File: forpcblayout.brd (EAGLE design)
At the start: 100 x 80 mm, 51 parts, among them J1 3x2 M, J2 S2B-PH-SM4-TB(LF)(SN), J3 629105136821, SW1 AYZ0202AGRLC, SW2 !RESET, U1 MCP73831, U2 MIC5219, U3 ATMEGA32U4-AUR, X2 16 MHz

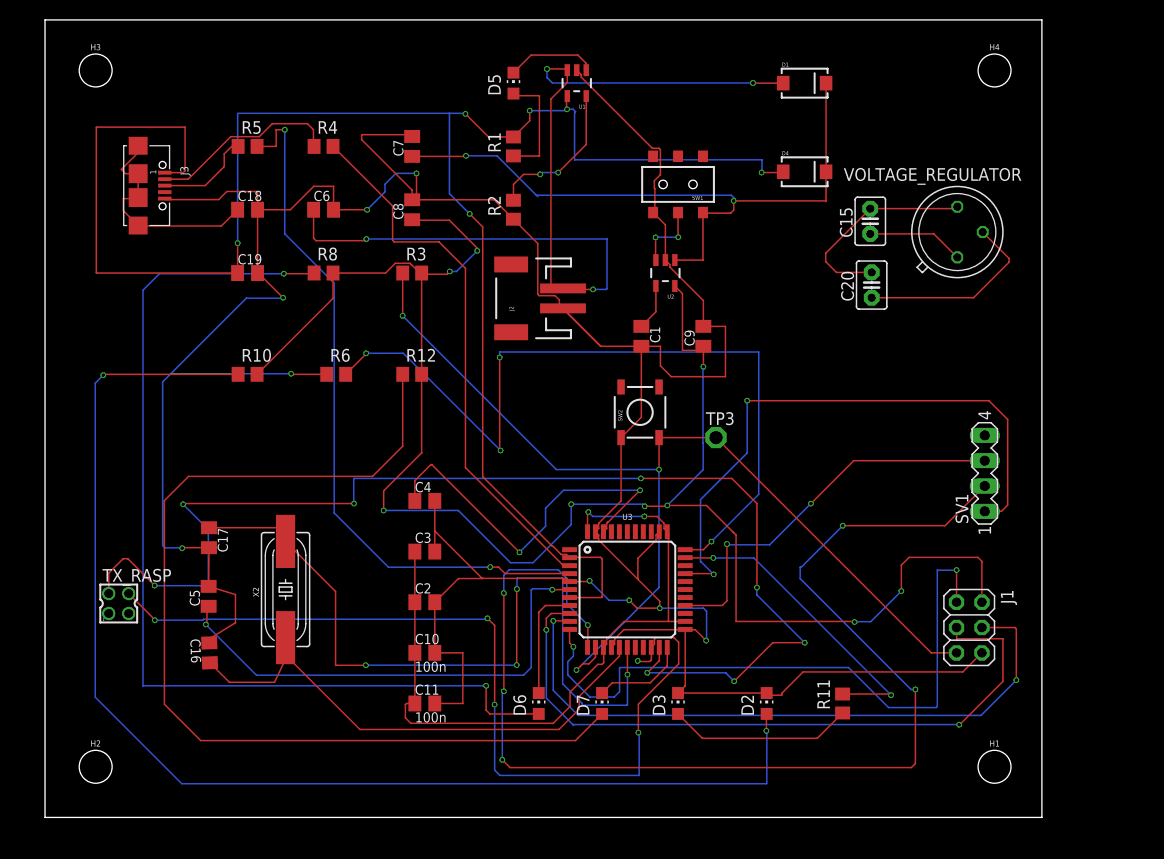
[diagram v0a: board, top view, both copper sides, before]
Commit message: PCB layout of schematic, and now has flooded gnds on both layers
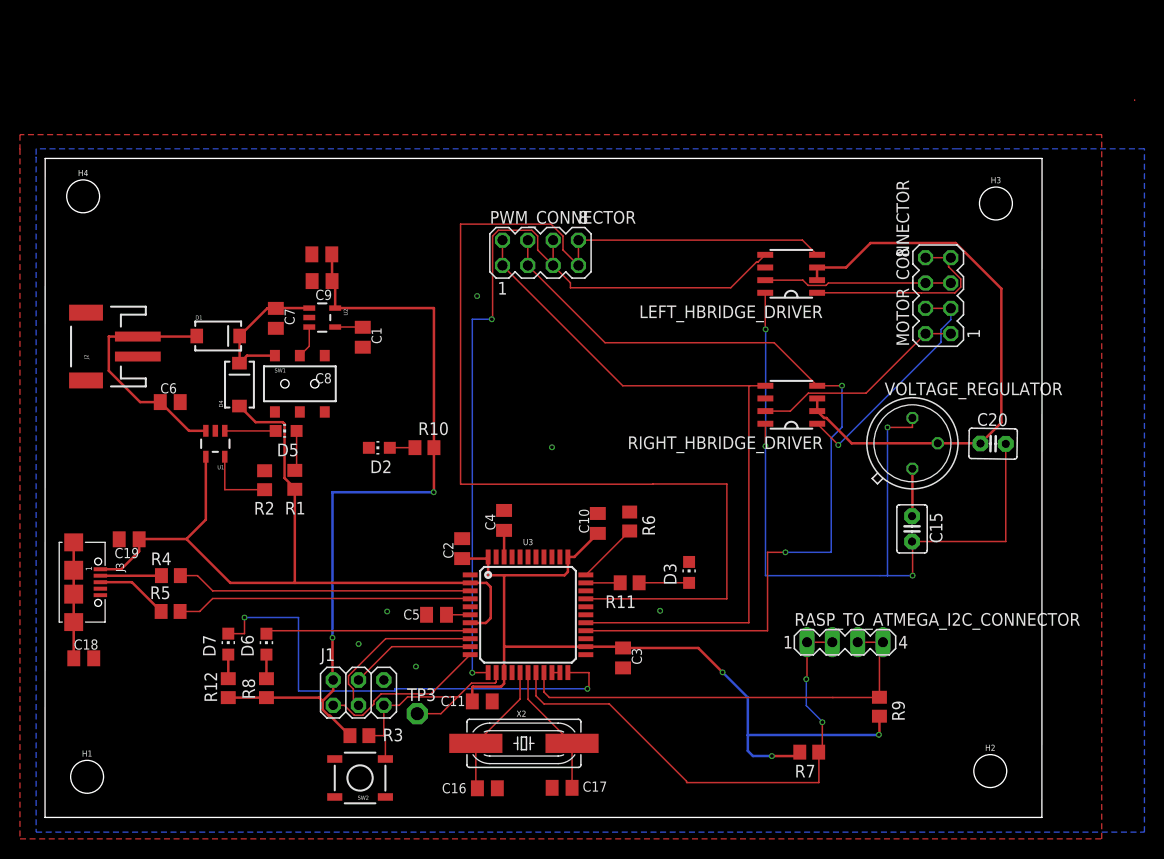
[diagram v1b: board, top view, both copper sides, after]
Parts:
- removed SV1: ATMEGA_DRIVER_CONNECTOR, con-lstb:MA04-1
- removed TX_RASP: RASP_TO_ATMEG_CONNECTOR, con-garry:332-04
- added LEFT_HBRIDGE_DRIVER, RIGHT_HBRIDGE_DRIVER: BD6230F, rohm:SOP8
- added MOTOR_CONNECTOR, PWM_CONNECTOR: (no value), con-lstb:MA04-2
- added R7, R9: 1K, rcl:R0805
- added RASP_TO_ATMEGA_I2C_CONNECTOR: (no value), con-lstb:MA04-1
- moved H4 92.3 mm to (3.82, 62.3)
- moved H3 91.3 mm to (95.4, 61.6)
- moved H1 91.0 mm to (4.22, 4.07)
- moved H2 89.7 mm to (94.8, 4.65)
- moved D1 64.1 mm to (17.4, 48.3)
- moved J1 61.6 mm to (31.4, 12.5), turned to 0 degrees
- moved D4 60.6 mm to (19.5, 43.4), turned to 90 degrees
- moved U1 51.2 mm to (17.1, 37.5)
- moved C18 47.9 mm to (3.88, 16.0)
- moved R5 47.3 mm to (12.6, 20.7)
- moved R3 46.7 mm to (31.5, 8.21), turned to 180 degrees
- moved D2 46.6 mm to (33.5, 37.1), turned to 90 degrees
- moved SW2 46.2 mm to (31.6, 3.96), turned to 180 degrees
- moved R4 45.7 mm to (12.6, 24.3)
- moved C17 43.4 mm to (51.9, 2.97), turned to 180 degrees
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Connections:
- removed net N$28: U3.18
- removed net N$29: U3.19
- removed net PWM_1?: SV1.1, U3.30
- removed net PWM_2?: SV1.2, U3.12
- removed net RX_ATMEGA?: TX_RASP.4, U3.20
- removed net TX_ATMEGA?: TX_RASP.2, U3.21
- new net LEFT_MOTOR1: LEFT_HBRIDGE_DRIVER.1, MOTOR_CONNECTOR.7, MOTOR_CONNECTOR.8
- new net LEFT_MOTOR2: LEFT_HBRIDGE_DRIVER.7, MOTOR_CONNECTOR.5, MOTOR_CONNECTOR.6
- new net NC: U3.20, U3.21
- new net PWM_1: LEFT_HBRIDGE_DRIVER.4, PWM_CONNECTOR.7, PWM_CONNECTOR.8, U3.30
- new net PWM_2: LEFT_HBRIDGE_DRIVER.5, PWM_CONNECTOR.5, PWM_CONNECTOR.6, U3.12
- new net RIGHT_MOTOR1: MOTOR_CONNECTOR.3, MOTOR_CONNECTOR.4, RIGHT_HBRIDGE_DRIVER.1
- new net RIGHT_MOTOR2: MOTOR_CONNECTOR.1, MOTOR_CONNECTOR.2, RIGHT_HBRIDGE_DRIVER.7
- new net SCL: R7.1, RASP_TO_ATMEGA_I2C_CONNECTOR.1, RASP_TO_ATMEGA_I2C_CONNECTOR.2, U3.18
- new net SDA: R9.1, RASP_TO_ATMEGA_I2C_CONNECTOR.3, RASP_TO_ATMEGA_I2C_CONNECTOR.4, U3.19
- net (5V@2.1A): now also R7.2, R9.2
- net 0: now also LEFT_HBRIDGE_DRIVER.8, RIGHT_HBRIDGE_DRIVER.8
- net H_BRIDGE_POWER: now also LEFT_HBRIDGE_DRIVER.2, LEFT_HBRIDGE_DRIVER.3, RIGHT_HBRIDGE_DRIVER.2, RIGHT_HBRIDGE_DRIVER.3
- net PWM_3: now also PWM_CONNECTOR.3, PWM_CONNECTOR.4, RIGHT_HBRIDGE_DRIVER.4; no longer SV1.3
- net PWM_4: now also PWM_CONNECTOR.1, PWM_CONNECTOR.2, RIGHT_HBRIDGE_DRIVER.5
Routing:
- net GND: track 360.4 -> 0.00 mm, vias 9 -> 0
- net PWM_2?: track 121.9 -> 0.00 mm, vias 6 -> 0
- net N$7: track 124.2 -> 2.53 mm, vias 2 -> 0
- net TX_ATMEGA?: track 120.9 -> 0.00 mm, vias 8 -> 0
- net PWM_1: track 0.00 -> 119.9 mm
- net VBUS: track 185.9 -> 79.2 mm, vias 6 -> 0
- net N$16: track 100.3 -> 2.42 mm
- net N$15: track 99.9 -> 2.42 mm, vias 2 -> 0
- net 3.3V: track 174.1 -> 80.1 mm, vias 9 -> 2
- net RX_ATMEGA?: track 88.9 -> 0.00 mm, vias 5 -> 0
- net PWM_2: track 0.00 -> 82.5 mm, vias 0 -> 2
- net !RESET: track 105.4 -> 25.0 mm, vias 3 -> 0
- net PE2/!HWB: track 80.3 -> 6.23 mm, vias 4 -> 0
- net PWM_4: track 0.00 -> 74.0 mm
- net V_BATT: track 92.7 -> 25.5 mm, vias 4 -> 0
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- added copper zone on layer 1, net GND
- added copper zone on layer 16, net GND
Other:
- board size 100 x 80 mm -> 100 x 66.1 mm

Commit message: Added in connector for Pi to ATMega as  well as battery for the schematic
Mounting holes line up (more or less) with the Pi now
We still need the right H Bridge Driver ICs, check GNDing, adding in vias for ea. GND connection, and check up on decoupling caps for power sources
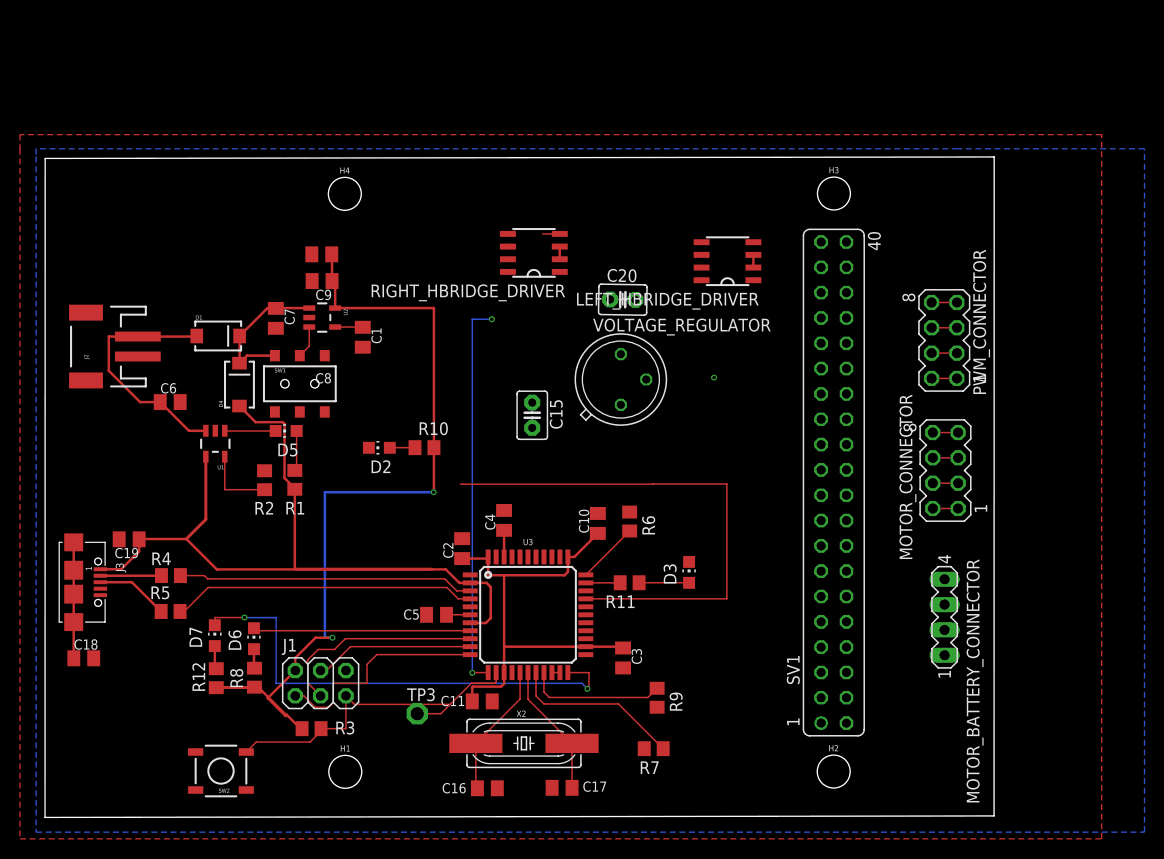
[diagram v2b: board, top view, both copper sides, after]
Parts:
- removed RASP_TO_ATMEGA_I2C_CONNECTOR: (no value), con-lstb:MA04-1
- added MOTOR_BATTERY_CONNECTOR: (no value), con-lstb:MA04-1
- added SV1: (no value), con-lsta:FE20-2
- VOLTAGE_REGULATOR: value 7805ABV -> LM7805ABV
- moved PWM_CONNECTOR 41.5 mm to (90.2, 47.8), turned to 90 degrees
- moved C20 39.9 mm to (58.0, 51.9)
- moved C15 39.8 mm to (48.9, 40.3)
- moved RIGHT_HBRIDGE_DRIVER 30.0 mm to (49.0, 56.6)
- moved VOLTAGE_REGULATOR 29.9 mm to (57.8, 43.9)
- moved H4 26.3 mm to (30.1, 62.6)
- moved H1 25.9 mm to (30.1, 4.57)
- moved R9 22.3 mm to (61.4, 12.0)
- moved MOTOR_CONNECTOR 17.6 mm to (90.3, 34.8)
- moved H3 16.3 mm to (79.1, 62.6)
- moved H2 15.7 mm to (79.1, 4.60)
- moved R7 15.6 mm to (61.1, 6.90)
- moved SW2 14.0 mm to (17.7, 4.66)
- moved LEFT_HBRIDGE_DRIVER 6.51 mm to (68.5, 55.8)
- moved R3 4.85 mm to (26.7, 8.91)
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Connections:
- removed net +5V: C15.1, VOLTAGE_REGULATOR.1
- removed net SCL: R7.1, RASP_TO_ATMEGA_I2C_CONNECTOR.1, RASP_TO_ATMEGA_I2C_CONNECTOR.2, U3.18
- new net 7.4V_FROM_BATT: C15.1, MOTOR_BATTERY_CONNECTOR.4, VOLTAGE_REGULATOR.1
- new net N$1: MOTOR_BATTERY_CONNECTOR.2, MOTOR_BATTERY_CONNECTOR.3
- new net N$2: PWM_CONNECTOR.7, PWM_CONNECTOR.8
- new net N$5: PWM_CONNECTOR.1, PWM_CONNECTOR.2
- new net N$6: PWM_CONNECTOR.3, PWM_CONNECTOR.4
- new net N$8: PWM_CONNECTOR.5, PWM_CONNECTOR.6
- new net POWER_IN: C10.1, C11.1, C2.1, C3.1, SV1.40, U3.14, U3.24, U3.34, U3.44
- new net SCLK: R7.1, SV1.35, U3.18
- net (5V@2.1A): no longer C10.1, C11.1, C2.1, C3.1, U3.14, U3.24, U3.34, U3.44
- net 0: no longer C15.2, C20.2, VOLTAGE_REGULATOR.3
- net GND: now also C15.2, C20.2, MOTOR_BATTERY_CONNECTOR.1, SV1.31, VOLTAGE_REGULATOR.3
- net PWM_1: no longer PWM_CONNECTOR.7, PWM_CONNECTOR.8
- net PWM_2: no longer PWM_CONNECTOR.5, PWM_CONNECTOR.6
- net PWM_3: no longer PWM_CONNECTOR.3, PWM_CONNECTOR.4
- net PWM_4: no longer PWM_CONNECTOR.1, PWM_CONNECTOR.2
- net SDA: now also SV1.37; no longer RASP_TO_ATMEGA_I2C_CONNECTOR.3, RASP_TO_ATMEGA_I2C_CONNECTOR.4
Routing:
- net PWM_3: track 88.7 -> 1.71 mm, vias 2 -> 0
- net 0: track 86.4 -> 0.00 mm, vias 4 -> 1
- net (5V@2.1A): track 86.3 -> 0.20 mm, vias 3 -> 0
- net PWM_4: track 74.0 -> 0.00 mm
- net PWM_1: track 119.9 -> 52.4 mm
- net H_BRIDGE_POWER: track 58.1 -> 2.74 mm
- net SCL: track 52.5 -> 0.00 mm, vias 2 -> 0
- net POWER_IN: track 0.00 -> 45.7 mm
- net PWM_2: track 82.5 -> 39.1 mm
- net SDA: track 44.1 -> 13.9 mm
- net RIGHT_MOTOR1: track 23.9 -> 2.54 mm, vias 1 -> 0
- net RIGHT_MOTOR2: track 21.8 -> 2.54 mm
- net LEFT_MOTOR1: track 20.7 -> 2.54 mm
- net SCLK: track 0.00 -> 17.3 mm
- net LEFT_MOTOR2: track 18.9 -> 2.54 mm
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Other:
- board size 100 x 66.1 mm -> 95.2 x 66.3 mm
